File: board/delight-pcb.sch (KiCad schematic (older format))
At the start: 171 parts, among them J1 AVR-ISP-6, SW0 KEYSW, SW1 KEYSW, SW10 KEYSW, SW11 KEYSW, SW12 KEYSW, SW13 KEYSW, SW14 KEYSW, SW15 KEYSW, SW16 KEYSW, SW17 KEYSW, SW18 KEYSW, SW19 KEYSW, SW2 KEYSW, SW20 KEYSW, SW21 KEYSW, SW22 KEYSW, SW23 KEYSW, SW24 KEYSW, SW25 KEYSW, SW26 KEYSW, SW27 KEYSW, SW28 KEYSW, SW28-2 KEYSW, SW29 KEYSW, SW3 KEYSW, SW30 KEYSW, SW31 KEYSW, SW32 KEYSW, SW33 KEYSW, SW34 KEYSW, SW35 KEYSW, SW36 KEYSW, SW37 KEYSW, SW38 KEYSW, SW39 KEYSW, SW4 KEYSW, SW40 KEYSW, SW41 KEYSW, SW42 KEYSW, SW42-2 KEYSW, SW43 KEYSW, SW44 KEYSW, SW44-2 KEYSW, SW45 KEYSW, SW46 KEYSW, SW47 KEYSW, SW48 KEYSW, SW49 KEYSW, SW5 KEYSW, SW50 KEYSW, SW51 KEYSW, SW52 KEYSW, SW53 KEYSW, SW54 KEYSW, SW55 KEYSW, SW56 KEYSW, SW57 KEYSW, SW58 KEYSW, SW59 KEYSW, SW59-2 KEYSW, SW6 KEYSW, SW60 KEYSW, SW60-2 KEYSW, SW61 KEYSW, SW62-2 KEYSW, SW63 KEYSW, SW63-2 KEYSW, SW64 KEYSW, SW64-2 KEYSW, SW65 KEYSW, SW65-2 KEYSW, SW66 KEYSW, SW67 KEYSW, SW68 KEYSW, SW69 KEYSW, SW7 KEYSW, SW8 KEYSW, SW9 KEYSW, U1 ATmega32A-PU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

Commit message: Updated all routes.
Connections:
- net row2: now also U1.20 (PD6); no longer U1.19 (PD5)
- net row3: now also U1.19 (PD5); no longer U1.20 (PD6)
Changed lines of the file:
@@
 Text GLabel 4575 8900 2    50   Input ~ 0
 row4
-Text GLabel 4575 10300 2    50   Input ~ 0
+Text GLabel 4575 10200 2    50   Input ~ 0
 row3
 Text GLabel 4575 10400 2    50   Input ~ 0
@@
 Text GLabel 4575 8800 2    50   Input ~ 0
 row1
-Text GLabel 4575 10200 2    50   Input ~ 0
+Text GLabel 4575 10300 2    50   Input ~ 0
 row2
 $EndSCHEMATC

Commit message: More cleanup
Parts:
- S62, SW44-2, SW59-2, SW60, SW61, SW64, SW65: footprint cftkb:SW_Cherry_MX1A_1.25u_PCBNOSCREEN -> cherrymx:SW_Cherry_MX_PCB_1.25u
- SW0, SW1, SW10, SW11, SW12, SW14, SW15, SW16, SW17, SW18, SW19, SW2, SW20, SW21, SW22, SW23, SW24, SW25, SW26, SW27, SW29, SW3, SW31, SW32, SW33, SW34, SW35, SW36, SW37, SW38, SW39, SW4, SW40, SW41, SW42-2, SW43, SW45, SW46, SW47, SW48, SW49, SW5, SW50, SW51, SW52, SW53, SW54, SW55, SW57, SW58, SW6, SW63, SW63-2, SW66, SW67, SW68, SW69, SW7, SW8, SW9: footprint cftkb:SW_Cherry_MX1A_1.00u_PCB-NOSCREEN -> cherrymx:SW_Cherry_MX_PCB_1.00u
- SW13: footprint cftkb:SW_Cherry_MX1A_2.00u_PCBNOSCREEN -> cherrymx:SW_Cherry_MX_PCB_2.00u
- SW28, SW30, SW60-2, SW62-2, SW64-2, SW65-2: footprint cftkb:SW_Cherry_MX1A_1.50u_PCBNOSCREEN -> cherrymx:SW_Cherry_MX_PCB_1.50u
- SW28-2: footprint cftkb:SW_Cherry_MX1A_ISOEnter_PCB_ReversedStabilizer -> cherrymx:SW_Cherry_MX_Plate_ISOEnter
- SW42, SW59: footprint cftkb:SW_Cherry_MX1A_2.25u_PCBNOSCREEN -> cherrymx:SW_Cherry_MX_PCB_2.25u
- SW44, SW56: footprint cftkb:SW_Cherry_MX1A_1.75u_PCBNOSCREEN -> cherrymx:SW_Cherry_MX_PCB_1.75u
- U1: footprint cftkb:DIP-40_W15.24mm -> Package_DIP:DIP-40_W15.24mm
- USB1: footprint cftkb:USB_C_GCT_USB4085 -> Connector_USB:USB_C_Receptacle_GCT_USB4085
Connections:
- net col0: now also SW0.2, SW15.2, SW30.2, SW44-2.2, SW44.2, SW59-2.2, SW59.2; no longer SW0.1, SW15.1, SW30.1, SW44-2.1, SW44.1, SW59-2.1, SW59.1
- net col1: now also SW1.2, SW16.2, SW31.2, SW45.2, SW60-2.2, SW60.2; no longer SW1.1, SW16.1, SW31.1, SW45.1, SW60-2.1, SW60.1
- net col10: now also SW10.2, SW25.2, SW40.2, SW54.2, SW65-2.2, SW65.2; no longer SW10.1, SW25.1, SW40.1, SW54.1, SW65-2.1, SW65.1
- net col11: now also SW11.2, SW26.2, SW41.2, SW55.2, SW66.2; no longer SW11.1, SW26.1, SW41.1, SW55.1, SW66.1
- net col12: now also SW12.2, SW27.2, SW56.2, SW67.2; no longer SW12.1, SW27.1, SW56.1, SW67.1
- net col13: now also SW13.2, SW28-2.2, SW28.2, SW42-2.2, SW42.2, SW57.2, SW68.2; no longer SW13.1, SW28-2.1, SW28.1, SW42-2.1, SW42.1, SW57.1, SW68.1
- net col14: now also SW14.2, SW29.2, SW43.2, SW58.2, SW69.2; no longer SW14.1, SW29.1, SW43.1, SW58.1, SW69.1
- net col2: now also SW17.2, SW2.2, SW32.2, SW46.2, SW61.2; no longer SW17.1, SW2.1, SW32.1, SW46.1, SW61.1
- net col3: now also S62.2, SW18.2, SW3.2, SW33.2, SW47.2, SW62-2.2; no longer S62.1, SW18.1, SW3.1, SW33.1, SW47.1, SW62-2.1
- net col4: now also SW19.2, SW34.2, SW4.2, SW48.2; no longer SW19.1, SW34.1, SW4.1, SW48.1
- net col5: now also SW20.2, SW35.2, SW49.2, SW5.2; no longer SW20.1, SW35.1, SW49.1, SW5.1
- net col6: now also SW21.2, SW36.2, SW50.2, SW6.2, SW63-2.2, SW63.2; no longer SW21.1, SW36.1, SW50.1, SW6.1, SW63-2.1, SW63.1
- net col7: now also SW22.2, SW37.2, SW51.2, SW7.2; no longer SW22.1, SW37.1, SW51.1, SW7.1
- net col8: now also SW23.2, SW38.2, SW52.2, SW8.2; no longer SW23.1, SW38.1, SW52.1, SW8.1
- net col9: now also SW24.2, SW39.2, SW53.2, SW64-2.2, SW64.2, SW9.2; no longer SW24.1, SW39.1, SW53.1, SW64-2.1, SW64.1, SW9.1
- net at D15.2 (A): now also SW15.1; no longer SW15.2
- net at D1.2 (A): now also SW1.1; no longer SW1.2
- net at D2.2 (A): now also SW2.1; no longer SW2.2
- net at D3.2 (A): now also SW3.1; no longer SW3.2
- net at D4.2 (A): now also SW4.1; no longer SW4.2
- net at D5.2 (A): now also SW5.1; no longer SW5.2
- net at D6.2 (A): now also SW6.1; no longer SW6.2
- net at D7.2 (A): now also SW7.1; no longer SW7.2
- net at D8.2 (A): now also SW8.1; no longer SW8.2
- net at D9.2 (A): now also SW9.1; no longer SW9.2
- net at D10.2 (A): now also SW10.1; no longer SW10.2
- net at D11.2 (A): now also SW11.1; no longer SW11.2
- net at D12.2 (A): now also SW12.1; no longer SW12.2
- net at D13.2 (A): now also SW13.1; no longer SW13.2
- net at D14.2 (A): now also SW14.1; no longer SW14.2
- net at D30.2 (A): now also SW30.1; no longer SW30.2
- net at D16.2 (A): now also SW16.1; no longer SW16.2
- net at D17.2 (A): now also SW17.1; no longer SW17.2
- net at D18.2 (A): now also SW18.1; no longer SW18.2
- net at D19.2 (A): now also SW19.1; no longer SW19.2
- net at D20.2 (A): now also SW20.1; no longer SW20.2
- net at D21.2 (A): now also SW21.1; no longer SW21.2
- net at D22.2 (A): now also SW22.1; no longer SW22.2
- net at D23.2 (A): now also SW23.1; no longer SW23.2
- net at D24.2 (A): now also SW24.1; no longer SW24.2
- net at D25.2 (A): now also SW25.1; no longer SW25.2
- net at D26.2 (A): now also SW26.1; no longer SW26.2
- net at D27.2 (A): now also SW27.1; no longer SW27.2
- net at D29.2 (A): now also SW29.1; no longer SW29.2
- net at D31.2 (A): now also SW31.1; no longer SW31.2
- net at D32.2 (A): now also SW32.1; no longer SW32.2
- net at D33.2 (A): now also SW33.1; no longer SW33.2
- net at D34.2 (A): now also SW34.1; no longer SW34.2
- net at D35.2 (A): now also SW35.1; no longer SW35.2
- net at D36.2 (A): now also SW36.1; no longer SW36.2
- net at D37.2 (A): now also SW37.1; no longer SW37.2
- net at D38.2 (A): now also SW38.1; no longer SW38.2
- net at D39.2 (A): now also SW39.1; no longer SW39.2
- net at D40.2 (A): now also SW40.1; no longer SW40.2
- net at D41.2 (A): now also SW41.1; no longer SW41.2
- net at D43.2 (A): now also SW43.1; no longer SW43.2
- net at D46.2 (A): now also SW46.1; no longer SW46.2
- net at D47.2 (A): now also SW47.1; no longer SW47.2
- net at D48.2 (A): now also SW48.1; no longer SW48.2
- net at D49.2 (A): now also SW49.1; no longer SW49.2
- net at D50.2 (A): now also SW50.1; no longer SW50.2
- net at D51.2 (A): now also SW51.1; no longer SW51.2
- net at D52.2 (A): now also SW52.1; no longer SW52.2
- net at D53.2 (A): now also SW53.1; no longer SW53.2
- net at D54.2 (A): now also SW54.1; no longer SW54.2
- net at D55.2 (A): now also SW55.1; no longer SW55.2
- net at D56.2 (A): now also SW56.1; no longer SW56.2
- net at D57.2 (A): now also SW57.1; no longer SW57.2
- net at D58.2 (A): now also SW58.1; no longer SW58.2
- net at D61.2 (A): now also SW61.1; no longer SW61.2
- net at D67.2 (A): now also SW67.1; no longer SW67.2
- net at D68.2 (A): now also SW68.1; no longer SW68.2
- net at D69.2 (A): now also SW69.1; no longer SW69.2
- net at D66.2 (A): now also SW66.1; no longer SW66.2
- net at D45.2 (A): now also SW45.1; no longer SW45.2
- net at D0.2 (A): now also SW0.1; no longer SW0.2
- new net: D28.2 (A), SW28-2.1, SW28.1
- new net: D44.2 (A), SW44-2.1, SW44.1
- new net: D42.2 (A), SW42-2.1, SW42.1
- new net: D59.2 (A), SW59-2.1, SW59.1
- new net: D60.2 (A), SW60-2.1, SW60.1
- new net: D62.2 (A), S62.1, SW62-2.1
- new net: D63.2 (A), SW63-2.1, SW63.1
- new net: D64.2 (A), SW64-2.1, SW64.1
- new net: D65.2 (A), SW65-2.1, SW65.1
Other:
- moved on the sheet: D0, D1, D10, D11, D12, D13, D14, D15, D16, D17, D18, D19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

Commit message: Adding Stabs back in.
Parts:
- F1: footprint cftkb:polyfuse_5.1mm -> project:Bourns-MF-R050-0-0-MFG
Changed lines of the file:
@@
 F 0 "F1" H 6718 6946 50  0000 L CNN
 F 1 "500mA" H 6718 6855 50  0000 L CNN
-F 2 "cftkb:polyfuse_5.1mm" H 6700 6700 50  0001 L CNN
+F 2 "project:Bourns-MF-R050-0-0-MFG" H 6700 6700 50  0001 L CNN
 F 3 "~" H 6650 6900 50  0001 C CNN
 	1    6650 6900

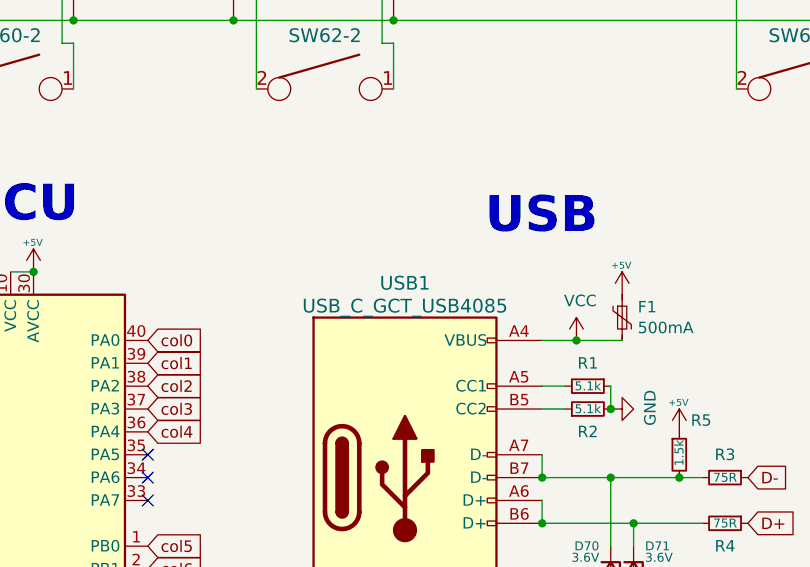
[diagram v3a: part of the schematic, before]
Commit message: Footprint schema updated
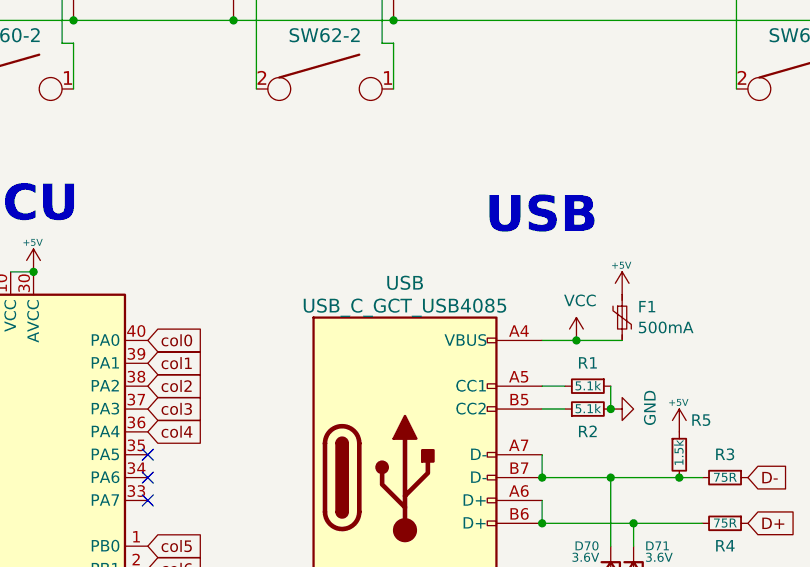
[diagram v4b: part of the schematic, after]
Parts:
- BOOT1, RESET1: footprint cftkb:SW_PUSH_6mm -> Button_Switch_THT:SW_PUSH_6mm
- C1, C2: footprint cftkb:C_Disc_D3.0mm_W1.6mm_P2.50mm -> Capacitor_THT:C_Disc_D3.0mm_W1.6mm_P2.50mm
- C3: footprint cftkb:CP_Radial_D4.0mm_P1.50mm -> Capacitor_THT:CP_Radial_D4.0mm_P1.50mm
- C4, C5: footprint cftkb:C_Disc_D4.3mm_W1.9mm_P5.00mm -> Capacitor_THT:C_Disc_D4.3mm_W1.9mm_P5.00mm
- D0, D1, D10, D11, D12, D13, D14, D15, D16, D17, D18, D19, D2, D20, D21, D22, D23, D24, D25, D26, D27, D28, D29, D3, D30, D31, D32, D33, D34, D35, D36, D37, D38, D39, D4, D40, D41, D42, D43, D44, D45, D46, D47, D48, D49, D5, D50, D51, D52, D53, D54, D55, D56, D57, D58, D59, D6, D60, D61, D62, D63, D64, D65, D66, D67, D68, D69, D7, D70, D71, D8, D9: footprint cftkb:D_DO-35_SOD27_P5.08mm_Horizontal -> Diode_THT:D_DO-35_SOD27_P7.62mm_Horizontal
- J1: footprint cftkb:AVR_ICSP_3x2 -> Connector_PinHeader_2.54mm:PinHeader_2x03_P2.54mm_Vertical
- LED1: footprint cftkb:LED_D3.0mm -> LED_THT:LED_D3.0mm
- R1, R2, R3, R4, R5, R6, R7: footprint cftkb:R_Axial_DIN0204_L3.6mm_D1.6mm_P5.08mm_Horizontal -> Resistor_THT:R_Axial_DIN0204_L3.6mm_D1.6mm_P5.08mm_Horizontal
- Y1: footprint cftkb:Crystal_HC49-4H_Vertical -> Crystal:Crystal_HC49-4H_Vertical
- renumbered USB1 to USB

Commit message: Once more with layouts
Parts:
- renumbered USB to USB1
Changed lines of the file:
@@
 $EndComp
 $Comp
-L delight-pcb-rescue:USB_C_Receptacle_USB2.0-Connector USB
+L delight-pcb-rescue:USB_C_Receptacle_USB2.0-Connector USB1
 U 1 1 5D127DE0
 P 5700 7600
-F 0 "USB" H 5700 8450 60  0000 C CNN
+F 0 "USB1" H 5700 8450 60  0000 C CNN
 F 1 "USB_C_GCT_USB4085" H 5700 8350 60  0000 C CNN
 F 2 "Connector_USB:USB_C_Receptacle_GCT_USB4085" H 5700 7600 60  0001 C CNN

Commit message: More project cleanup
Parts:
- F1: footprint project:Bourns-MF-R050-0-0-MFG -> Fuse:Fuse_Bourns_MF-RHT050
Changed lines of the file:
@@
 F 0 "F1" H 6718 6946 50  0000 L CNN
 F 1 "500mA" H 6718 6855 50  0000 L CNN
-F 2 "project:Bourns-MF-R050-0-0-MFG" H 6700 6700 50  0001 L CNN
+F 2 "Fuse:Fuse_Bourns_MF-RHT050" H 6700 6700 50  0001 L CNN
 F 3 "~" H 6650 6900 50  0001 C CNN
 	1    6650 6900

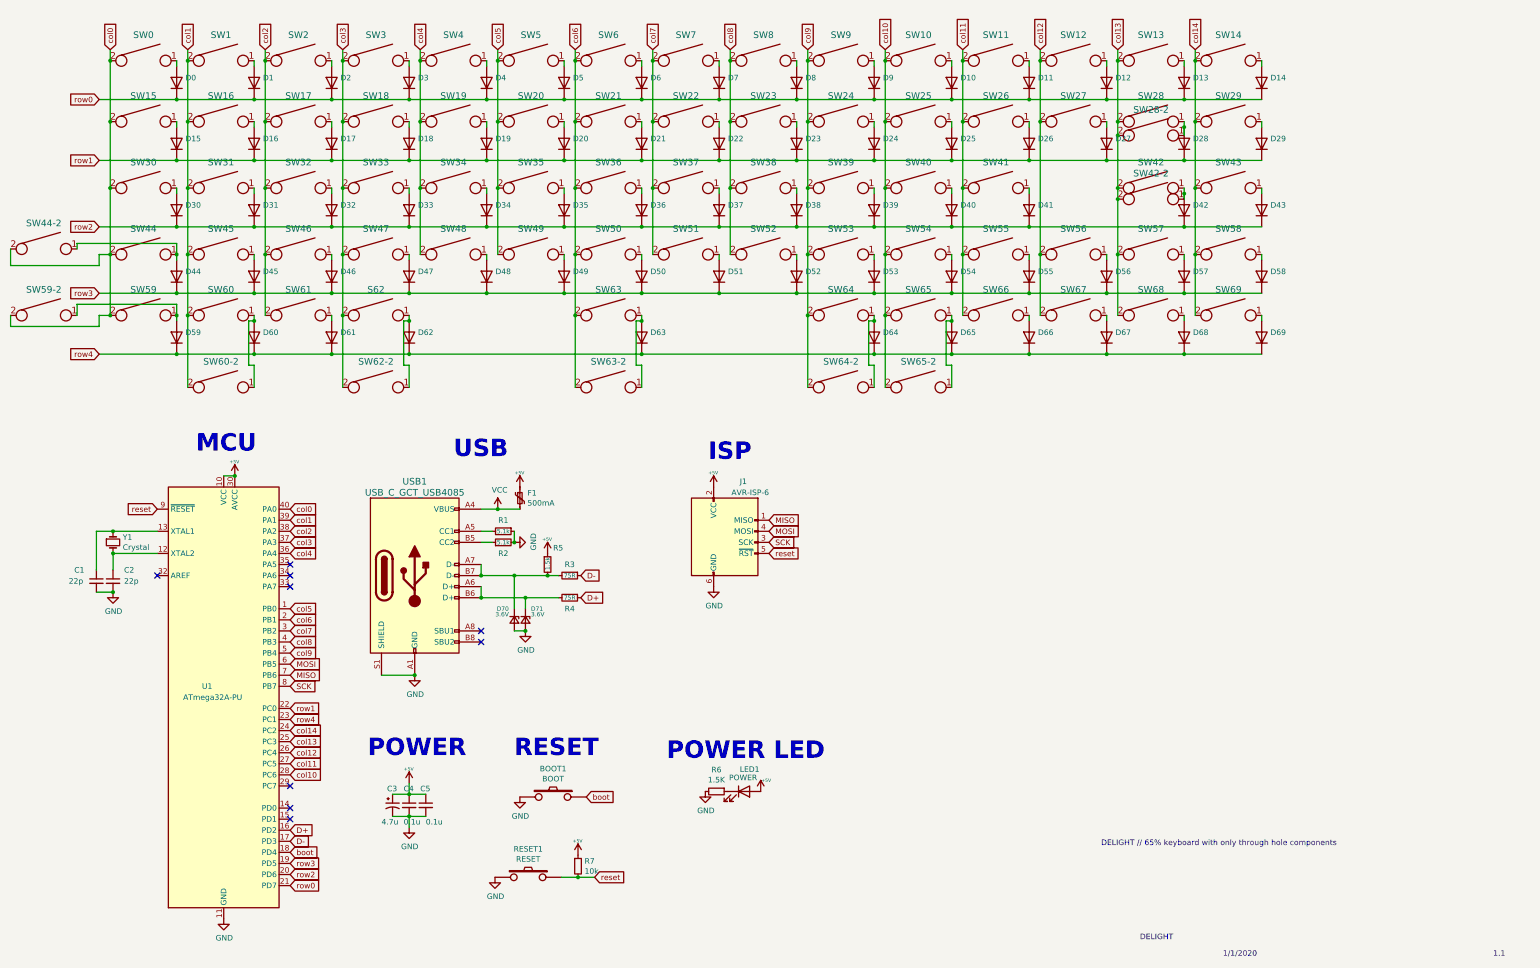
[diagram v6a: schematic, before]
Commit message: Hotswap created and routed
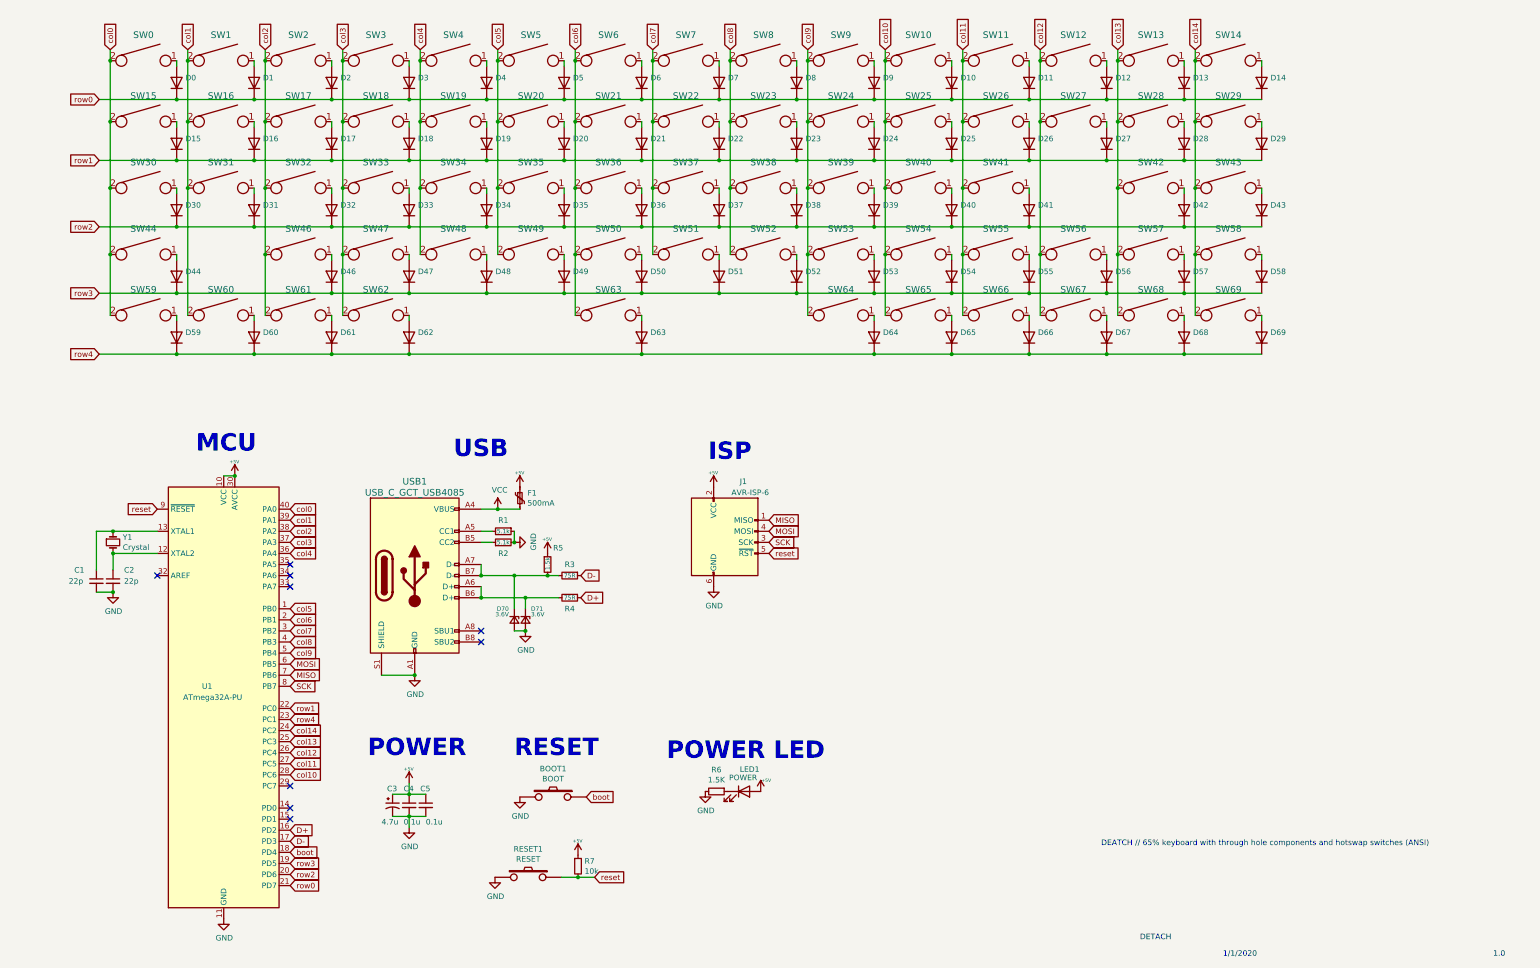
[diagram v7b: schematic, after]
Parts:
- removed D45: (no value), Diode_THT:D_DO-35_SOD27_P7.62mm_Horizontal, symbol delight-pcb-rescue:D-Device
- removed SW28-2: KEYSW, cherrymx:SW_Cherry_MX_Plate_ISOEnter, symbol delight-pcb-rescue:KEYSW-keyboard_parts
- removed SW42-2, SW45, SW63-2: KEYSW, cherrymx:SW_Cherry_MX_PCB_1.00u, symbol delight-pcb-rescue:KEYSW-keyboard_parts
- removed SW44-2, SW59-2: KEYSW, cherrymx:SW_Cherry_MX_PCB_1.25u, symbol delight-pcb-rescue:KEYSW-keyboard_parts
- removed SW60-2, SW62-2, SW64-2, SW65-2: KEYSW, cherrymx:SW_Cherry_MX_PCB_1.50u, symbol delight-pcb-rescue:KEYSW-keyboard_parts
- SW0, SW1, SW10, SW11, SW12, SW14, SW15, SW16, SW17, SW18, SW19, SW2, SW20, SW21, SW22, SW23, SW24, SW25, SW26, SW27, SW29, SW3, SW31, SW32, SW33, SW34, SW35, SW36, SW37, SW38, SW39, SW4, SW40, SW41, SW43, SW46, SW47, SW48, SW49, SW5, SW50, SW51, SW52, SW53, SW54, SW55, SW57, SW58, SW6, SW66, SW67, SW68, SW69, SW7, SW8, SW9: footprint cherrymx:SW_Cherry_MX_PCB_1.00u -> Switch_Keyboard_Kailh:SW_Hotswap_Kailh_1.00u
- SW13: footprint cherrymx:SW_Cherry_MX_PCB_2.00u -> Switch_Keyboard_Kailh:SW_Hotswap_Kailh_2.00u
- SW28, SW30: footprint cherrymx:SW_Cherry_MX_PCB_1.50u -> Switch_Keyboard_Kailh:SW_Hotswap_Kailh_1.50u
- SW42, SW59: footprint cherrymx:SW_Cherry_MX_PCB_2.25u -> Switch_Keyboard_Kailh:SW_Hotswap_Kailh_2.25u
- SW44, SW56: footprint cherrymx:SW_Cherry_MX_PCB_1.75u -> Switch_Keyboard_Kailh:SW_Hotswap_Kailh_1.75u
- SW60, SW61: footprint cherrymx:SW_Cherry_MX_PCB_1.25u -> Switch_Keyboard_Kailh:SW_Hotswap_Kailh_1.25u
- SW62: renamed from S62; footprint cherrymx:SW_Cherry_MX_PCB_1.25u -> Switch_Keyboard_Kailh:SW_Hotswap_Kailh_1.25u
- SW63: footprint cherrymx:SW_Cherry_MX_PCB_1.00u -> Switch_Keyboard_Kailh:SW_Hotswap_Kailh_6.25u
- SW64, SW65: footprint cherrymx:SW_Cherry_MX_PCB_1.25u -> Switch_Keyboard_Kailh:SW_Hotswap_Kailh_1.00u
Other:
- note added: "1.0"
- note added: "DEATCH // 65% keyboard with through hole components and hotswap switches (ANSI)"
- note added: "DETACH"
- note removed: "1.1"
- note removed: "DELIGHT"
- note removed: "DELIGHT // 65% keyboard with only through hole components"
